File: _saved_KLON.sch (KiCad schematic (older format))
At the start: 69 parts, among them IC1 MAX1044ESA+, SW1 3PDT, U1 TL072, U2 TL072

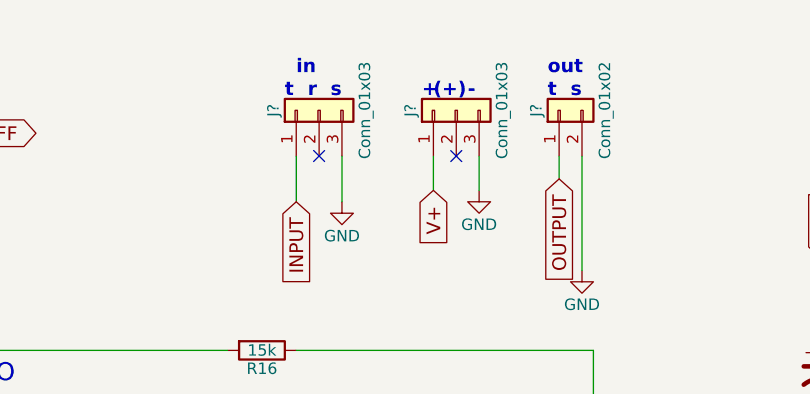
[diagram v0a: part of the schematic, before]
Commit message: Changed connectors for in, out, power. Added footprints for several parts. Correlated footprints to parts. Started PCB.
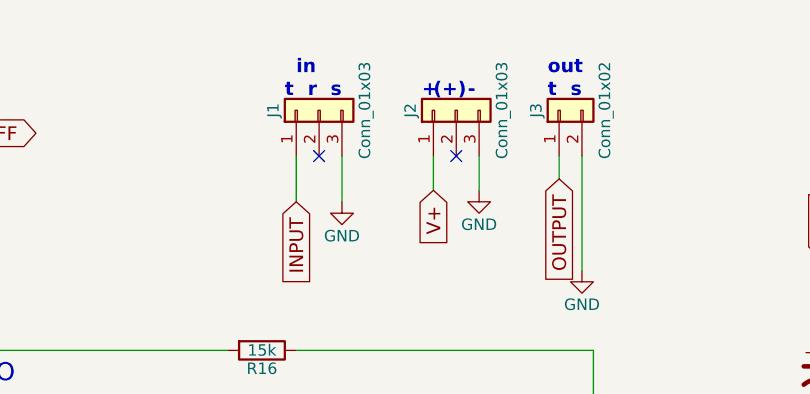
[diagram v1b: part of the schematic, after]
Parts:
- J1, J2: renamed from J?; footprint (none) -> Socket_Strips:Socket_Strip_Straight_1x03_Pitch2.54mm
- J3: renamed from J?; footprint (none) -> Socket_Strips:Socket_Strip_Straight_1x02_Pitch2.54mm
- Z1: footprint DIOAD1413W86L463D238 -> projectfootprints:DIODEAD1413W86L463D238
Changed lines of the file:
@@
 LIBS:contrib
 LIBS:valves
-LIBS:dk_USB-DVI-HDMI-Connectors
-LIBS:dk_TVS-Mixed-Technology
-LIBS:dk_TVS-Diodes
-LIBS:dk_Trimmer-Potentiometers
-LIBS:dk_Transistors-JFETs
-LIBS:dk_Transistors-FETs-MOSFETs-Single
-LIBS:dk_Transistors-FETs-MOSFETs-RF
-LIBS:dk_Transistors-FETs-MOSFETs-Arrays
-LIBS:dk_Transistors-Bipolar-BJT-Single
-LIBS:dk_Transistors-Bipolar-BJT-Single-Pre-Biased
-LIBS:dk_Transistors-Bipolar-BJT-RF
-LIBS:dk_Transistors-Bipolar-BJT-Arrays
-LIBS:dk_Toggle-Switches
-LIBS:dk_Thyristors-TRIACs
-LIBS:dk_Thyristors-SCRs
-LIBS:dk_Thyristors-DIACs-SIDACs
-LIBS:dk_Thermal-Cutoffs-Thermal-Fuses
-LIBS:dk_Temperature-Sensors-Analog-and-Digital-Output
-LIBS:dk_Tactile-Switches
-LIBS:dk_Surge-Suppression-ICs
-LIBS:dk_Specialized-Sensors
-LIBS:dk_Specialized-ICs
-LIBS:dk_Solid-State-Relays
-LIBS:dk_Slide-Switches
-LIBS:dk_Signal-Relays-Up-to-2-Amps
-LIBS:dk_Sensors-Transducers_Accessories
-LIBS:dk_Rotary-Potentiometers-Rheostats
-LIBS:dk_RFID-RF-Access-Monitoring-ICs
-LIBS:dk_RF-Transmitters
-LIBS:dk_RF-Transceiver-Modules
-LIBS:dk_RF-Transceiver-ICs
-LIBS:dk_RF-Switches
-LIBS:dk_RF-Receivers
-LIBS:dk_RF-Evaluation-and-Development-Kits-Boards
-LIBS:dk_RF-Detectors
-LIBS:dk_RF-Demodulators
-LIBS:dk_RF-Antennas
-LIBS:dk_RF-Amplifiers
-LIBS:dk_Resistor-Networks-Arrays
-LIBS:dk_Reed-Relays
-LIBS:dk_Rectangular-Connectors-Headers-Male-Pins
-LIBS:dk_Pushbutton-Switches
-LIBS:dk_Programmable-Oscillators
-LIBS:dk_Pressure-Sensors-Transducers
-LIBS:dk_Power-Relays-Over-2-Amps
-LIBS:dk_PMIC-Voltage-Regulators-Special-Purpose
-LIBS:dk_PMIC-Voltage-Regulators-Linear
-LIBS:dk_PMIC-Voltage-Regulators-DC-DC-Switching-Regulators
-LIBS:dk_PMIC-Voltage-Regulators-DC-DC-Switching-Controllers
-LIBS:dk_PMIC-Voltage-Reference
-LIBS:dk_PMIC-V-F-and-F-V-Converters
-LIBS:dk_PMIC-Thermal-Management
-LIBS:dk_PMIC-Supervisors
-LIBS:dk_PMIC-RMS-to-DC-Converters
-LIBS:dk_PMIC-Power-Management-Specialized
-LIBS:dk_PMIC-Power-Distribution-Switches-Load-Drivers
-LIBS:dk_PMIC-OR-Controllers-Ideal-Diodes
-LIBS:dk_PMIC-Motor-Drivers-Controllers
-LIBS:dk_PMIC-LED-Drivers
-LIBS:dk_PMIC-Gate-Drivers
-LIBS:dk_PMIC-Full-Half-Bridge-Drivers
-LIBS:dk_PMIC-Current-Regulation-Management
-LIBS:dk_PMIC-Battery-Management
-LIBS:dk_PMIC-Battery-Chargers
-LIBS:dk_PMIC-AC-DC-Converters-Offline-Switchers
-LIBS:dk_Oscillators
-LIBS:dk_Optoisolators-Triac-SCR-Output
-LIBS:dk_Optoisolators-Transistor-Photovoltaic-Output
-LIBS:dk_Optoisolators-Logic-Output
-LIBS:dk_Optical-Sensors-Reflective-Analog-Output
-LIBS:dk_Optical-Sensors-Phototransistors
-LIBS:dk_Optical-Sensors-Photodiodes
-LIBS:dk_Optical-Sensors-Photo-Detectors-Remote-Receiver
-LIBS:dk_Optical-Sensors-Ambient-Light-IR-UV-Sensors
-LIBS:dk_Navigation-Switches-Joystick
-LIBS:dk_Motion-Sensors-Tilt-Switches
-LIBS:dk_Motion-Sensors-IMUs-Inertial-Measurement-Units
-LIBS:dk_Motion-Sensors-Accelerometers
-LIBS:dk_Modular-Connectors-Jacks
-LIBS:dk_Modular-Connectors-Jacks-With-Magnetics
-LIBS:dk_Microphones
-LIBS:dk_Memory
-LIBS:dk_Memory-Connectors-PC-Card-Sockets
-LIBS:dk_Magnetic-Sensors-Switches-Solid-State
-LIBS:dk_Magnetic-Sensors-Linear-Compass-ICs
-LIBS:dk_Magnetic-Sensors-Compass-Magnetic-Field-Modules
-LIBS:dk_Logic-Translators-Level-Shifters
-LIBS:dk_Logic-Signal-Switches-Multiplexers-Decoders
-LIBS:dk_Logic-Shift-Registers
-LIBS:dk_Logic-Multivibrators
-LIBS:dk_Logic-Gates-and-Inverters
-LIBS:dk_Logic-Flip-Flops
-LIBS:dk_Logic-Buffers-Drivers-Receivers-Transceivers
-LIBS:dk_Linear-Comparators
-LIBS:dk_Linear-Amplifiers-Instrumentation-OP-Amps-Buffer-Amps
-LIBS:dk_Linear-Amplifiers-Audio
-LIBS:dk_LEDs-Circuit-Board-Indicators-Arrays-Light-Bars-Bar-Graphs
-LIBS:dk_LED-Indication-Discrete
-LIBS:dk_Interface-Specialized
-LIBS:dk_Interface-Sensor-Capacitive-Touch
-LIBS:dk_Interface-Sensor-and-Detector-Interfaces
-LIBS:dk_Interface-Modules
-LIBS:dk_Interface-I-O-Expanders
-LIBS:dk_Interface-Drivers-Receivers-Transceivers
-LIBS:dk_Interface-Controllers
-LIBS:dk_Interface-Analog-Switches-Special-Purpose
-LIBS:dk_Interface-Analog-Switches-Multiplexers-Demultiplexers
-LIBS:dk_Inrush-Current-Limiters-ICL
-LIBS:dk_Infrared-UV-Visible-Emitters
-LIBS:dk_Image-Sensors-Camera
-LIBS:dk_Humidity-Moisture-Sensors
-LIBS:dk_Gas-Sensors
-LIBS:dk_Fuses
-LIBS:dk_Fixed-Inductors
-LIBS:dk_Ferrite-Beads-and-Chips
-LIBS:dk_Evaluation-Boards-Sensors
-LIBS:dk_Encoders
-LIBS:dk_Embedded-Microcontrollers
-LIBS:dk_Display-Modules-LED-Character-and-Numeric
-LIBS:dk_Diodes-Zener-Single
-LIBS:dk_Diodes-Rectifiers-Single
-LIBS:dk_Diodes-Rectifiers-Arrays
-LIBS:dk_Diodes-Bridge-Rectifiers
-LIBS:dk_Digital-Isolators
-LIBS:dk_DC-DC-Converters
-LIBS:dk_Data-Acquisition-Touch-Screen-Controllers
-LIBS:dk_Data-Acquisition-Digital-to-Analog-Converters-DAC
-LIBS:dk_Data-Acquisition-Digital-Potentiometers
-LIBS:dk_Data-Acquisition-Analog-to-Digital-Converters-ADC
-LIBS:dk_Data-Acquisition-ADCs-DACs-Special-Purpose
-LIBS:dk_D-Sub-Connectors
-LIBS:dk_Current-Transducers
-LIBS:dk_Coaxial-Connectors-RF
-LIBS:dk_Clock-Timing-Real-Time-Clocks
-LIBS:dk_Clock-Timing-Programmable-Timers-and-Oscillators
-LIBS:dk_Clock-Timing-Clock-Generators-PLLs-Frequency-Synthesizers
-LIBS:dk_Battery-Holders-Clips-Contacts
-LIBS:dk_Barrel-Audio-Connectors
-LIBS:dk_Balun
-LIBS:dk_Automotive-Relays
-LIBS:dk_Alarms-Buzzers-and-Sirens
-LIBS:dk_Addressable-Specialty
 LIBS:3PDT
 LIBS:MAX1044ESA+
@@
 F 0 "Z1" H 7950 550 50  0000 L BNN
 F 1 "1N4742ATR" H 7800 900 50  0000 L BNN
-F 2 "DIOAD1413W86L463D238" H 8050 900 50  0001 L BNN
+F 2 "projectfootprints:DIODEAD1413W86L463D238" H 8050 900 50  0001 L BNN
 F 3 "http://uk.rs-online.com/web/p/products/8050075" H 8050 800 50  0001 L BNN
 F 4 "Diode, Fairchild, 1N4742ATR Fairchild 1N4742ATR Zener Diode, 12V 5% 1 W Through Hole 2-Pin DO-41" H 8050 700 50  0001 L BNN "Description"
@@
 NoConn ~ 1600 6950
 $Comp
-L Conn_01x03 J?
+L Conn_01x03 J1
 U 1 1 5AB73706
 P 4850 800
-F 0 "J?" H 4850 1000 50  0000 C CNN
+F 0 "J1" H 4850 1000 50  0000 C CNN
 F 1 "Conn_01x03" H 4850 600 50  0000 C CNN
-F 2 "" H 4850 800 50  0001 C CNN
+F 2 "Socket_Strips:Socket_Strip_Straight_1x03_Pitch2.54mm" H 4850 800 50  0001 C CNN
 F 3 "" H 4850 800 50  0001 C CNN
 	1    4850 800
@@
 $EndComp
 $Comp
-L Conn_01x03 J?
+L Conn_01x03 J2
 U 1 1 5AB73817
 P 5450 800
-F 0 "J?" H 5450 1000 50  0000 C CNN
+F 0 "J2" H 5450 1000 50  0000 C CNN
 F 1 "Conn_01x03" H 5450 600 50  0000 C CNN
-F 2 "" H 5450 800 50  0001 C CNN
+F 2 "Socket_Strips:Socket_Strip_Straight_1x03_Pitch2.54mm" H 5450 800 50  0001 C CNN
 F 3 "" H 5450 800 50  0001 C CNN
 	1    5450 800
@@
 $EndComp
 $Comp
-L Conn_01x02 J?
+L Conn_01x02 J3
 U 1 1 5AB739F0
 P 5900 800
-F 0 "J?" H 5900 900 50  0000 C CNN
+F 0 "J3" H 5900 900 50  0000 C CNN
 F 1 "Conn_01x02" H 5900 600 50  0000 C CNN
-F 2 "" H 5900 800 50  0001 C CNN
+F 2 "Socket_Strips:Socket_Strip_Straight_1x02_Pitch2.54mm" H 5900 800 50  0001 C CNN
 F 3 "" H 5900 800 50  0001 C CNN
 	1    5900 800
